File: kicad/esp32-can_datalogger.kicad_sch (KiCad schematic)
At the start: 22 parts, among them J1 USB_C_Receptacle_USB2.0_16P, J2 USB_C_Receptacle_USB2.0_16P, J3 USB_C_Receptacle_USB2.0_16P, J4 USB_C_Receptacle_USB2.0_16P, J5 MSD-4-A, U5 TJA1051T, U6 TJA1051T

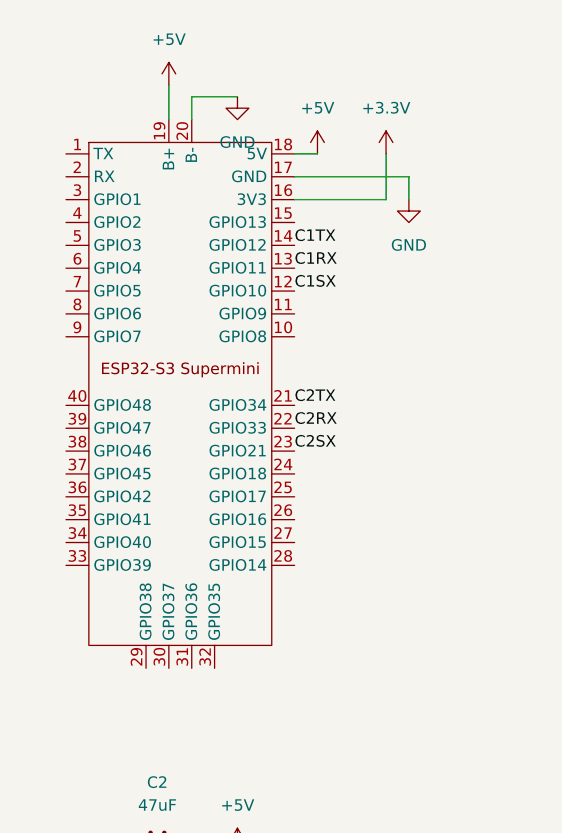
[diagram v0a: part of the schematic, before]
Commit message: switch to esp32-c6
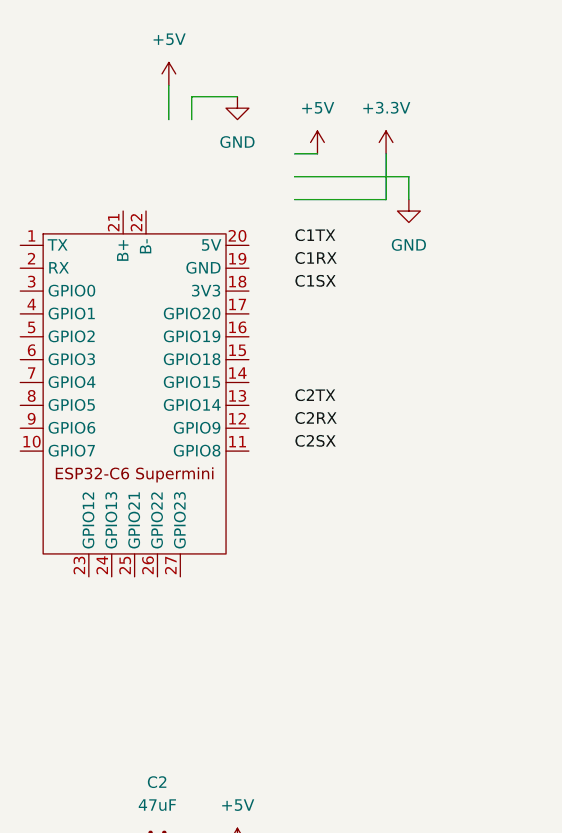
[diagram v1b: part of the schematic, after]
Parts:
- removed U1: (no value), esp32-can_datalogger:ESP32-S3 Supermini, symbol esp32-can_datalogger:esp32-s3-supermini
- added U1: (no value), esp32-can_datalogger:ESP32-C6 Supermini, symbol esp32-can_datalogger:esp32-c6-supermini
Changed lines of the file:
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@@
+	)
+	(symbol
+		(lib_id "esp32-can_datalogger:esp32-c6-supermini")
+		(at 31.75 57.15 0)
+		(unit 1)
+		(body_style 1)
+		(exclude_from_sim no)
+		(in_bom yes)
+		(on_board yes)
+		(in_pos_files yes)
+		(dnp no)
+		(fields_autoplaced yes)
+		(property "Reference" "U1"
+			(at 31.75 62.23 0)
+			(hide yes)
+			(show_name no)
+			(do_not_autoplace no)
+			(effects
+				(font
+					(size 1.27 1.27)
+				)
+			)
+		)
+		(property "Value" ""
+			(at 31.75 62.23 0)
+			(hide yes)
+			(show_name no)
+			(do_not_autoplace no)
+			(effects
+				(font
+					(size 1.27 1.27)
+				)
+			)
+		)
+		(property "Footprint" "esp32-can_datalogger:ESP32-C6 Supermini"
+			(at 31.75 62.23 0)
+			(hide yes)
+			(show_name no)
+			(do_not_autoplace no)
+			(effects
+				(font
+					(size 1.27 1.27)
+				)
+			)
+		)
+		(property "Datasheet" ""
+			(at 31.75 62.23 0)
+			(hide yes)
+			(show_name no)
+			(do_not_autoplace no)
+			(effects
+				(font
+					(size 1.27 1.27)
+				)
+			)
+		)
+		(property "Description" ""
+			(at 31.75 62.23 0)
+			(hide yes)
+			(show_name no)
+			(do_not_autoplace no)
+			(effects
+				(font
+					(size 1.27 1.27)
+				)
+			)
+		)
+		(pin "4"
+		)
+		(pin "5"
+		)
+		(pin "24"
+		)
+		(pin "26"
+		)
+		(pin "7"
+		)
+		(pin "21"
+		)
+		(pin "22"
+		)
+		(pin "12"
+		)
+		(pin "16"
+		)
+		(pin "27"
+		)
+		(pin "20"
+		)
+		(pin "17"
+		)
+		(pin "6"
+		)
+		(pin "9"
+		)
+		(pin "11"
+		)
+		(pin "13"
+		)
+		(pin "15"
+		)
+		(pin "19"
+		)
+		(pin "23"
+		)
+		(pin "10"
+		)
+		(pin "14"
+		)
+		(pin "18"
+		)
+		(pin "8"
+		)
+		(pin "25"
+		)
+		(pin "2"
+		)
+		(pin "3"
+		)
+		(pin "1"
+		)
+		(instances
+			(project "esp32-can_datalogger"
+				(path "/27d88dad-6a90-4f6f-a0dd-ec7ff61f0111"
+					(reference "U1")
+					(unit 1)
+				)
+			)
+		)
 	)
 	(symbol
@@
 					(unit 1)
 				)
-			)
-		)
-	)
-	(symbol
-		(lib_id "esp32-can_datalogger:esp32-s3-supermini")
-		(at 36.83 54.61 0)
-		(unit 1)
-		(body_style 1)
-		(exclude_from_sim no)
-		(in_bom yes)
-		(on_board yes)
-		(in_pos_files yes)
-		(dnp no)
-		(fields_autoplaced yes)
-		(property "Reference" "U1"
-			(at 36.83 52.07 0)
-			(hide yes)
-			(show_name no)
-			(do_not_autoplace no)
-			(effects
-				(font
-					(size 1.27 1.27)
-				)
-			)
-		)
-		(property "Value" ""
-			(at 36.83 52.07 0)
-			(hide yes)
-			(show_name no)
-			(do_not_autoplace no)
-			(effects
-				(font
-					(size 1.27 1.27)
-				)
-			)
-		)
-		(property "Footprint" "esp32-can_datalogger:ESP32-S3 Supermini"
-			(at 36.83 52.07 0)
-			(hide yes)
-			(show_name no)
-			(do_not_autoplace no)
-			(effects
-				(font
-					(size 1.27 1.27)
-				)
-			)
-		)
-		(property "Datasheet" ""
-			(at 36.83 52.07 0)
-			(hide yes)
-			(show_name no)
-			(do_not_autoplace no)
-			(effects
-				(font
-					(size 1.27 1.27)
-				)
-			)
-		)
-		(property "Description" ""
-			(at 36.83 52.07 0)
-			(hide yes)
-			(show_name no)
-			(do_not_autoplace no)
-			(effects
-				(font
-					(size 1.27 1.27)
-				)
-			)
-		)
-		(pin "19"
-		)
-		(pin "9"
-		)
-		(pin "13"
-		)
-		(pin "14"
-		)
-		(pin "10"
-		)
-		(pin "6"
-		)
-		(pin "5"
-		)
-		(pin "2"
-		)
-		(pin "4"
-		)
-		(pin "3"
-		)
-		(pin "1"
-		)
-		(pin "7"
-		)
-		(pin "11"
-		)
-		(pin "12"
-		)
-		(pin "15"
-		)
-		(pin "16"
-		)
-		(pin "17"
-		)
-		(pin "18"
-		)
-		(pin "8"
-		)
-		(pin "29"
-		)
-		(pin "21"
-		)
-		(pin "26"
-		)
-		(pin "20"
-		)
-		(pin "28"
-		)
-		(pin "23"
-		)
-		(pin "27"
-		)
-		(pin "22"
-		)
-		(pin "24"
-		)
-		(pin "25"
-		)
-		(pin "30"
-		)
-		(pin "32"
-		)
-		(pin "33"
-		)
-		(pin "35"
-		)
-		(pin "34"
-		)
-		(pin "36"
-		)
-		(pin "31"
-		)
-		(pin "40"
-		)
-		(pin "37"
-		)
-		(pin "39"
-		)
-		(pin "38"
-		)
-		(instances
-			(project "esp32-can_datalogger"
-				(path "/27d88dad-6a90-4f6f-a0dd-ec7ff61f0111"
-					(reference "U1")
-					(unit 1)
-				)

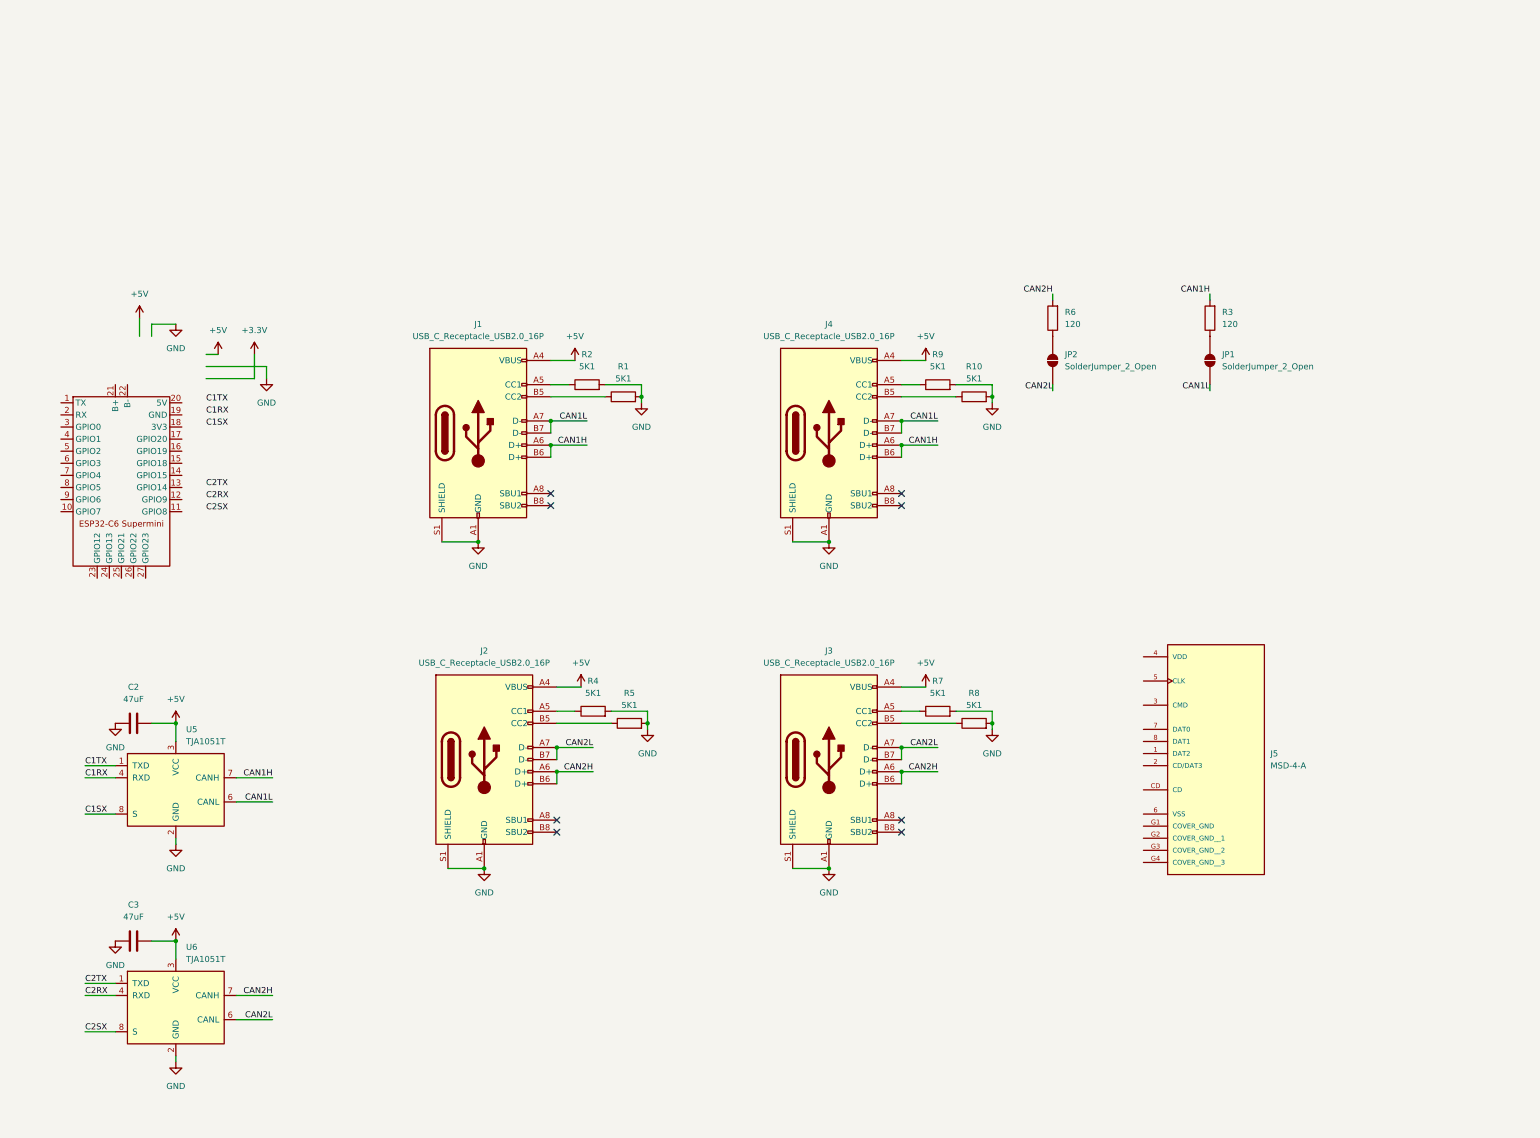
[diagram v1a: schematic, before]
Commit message: add gps, imu to board schematic
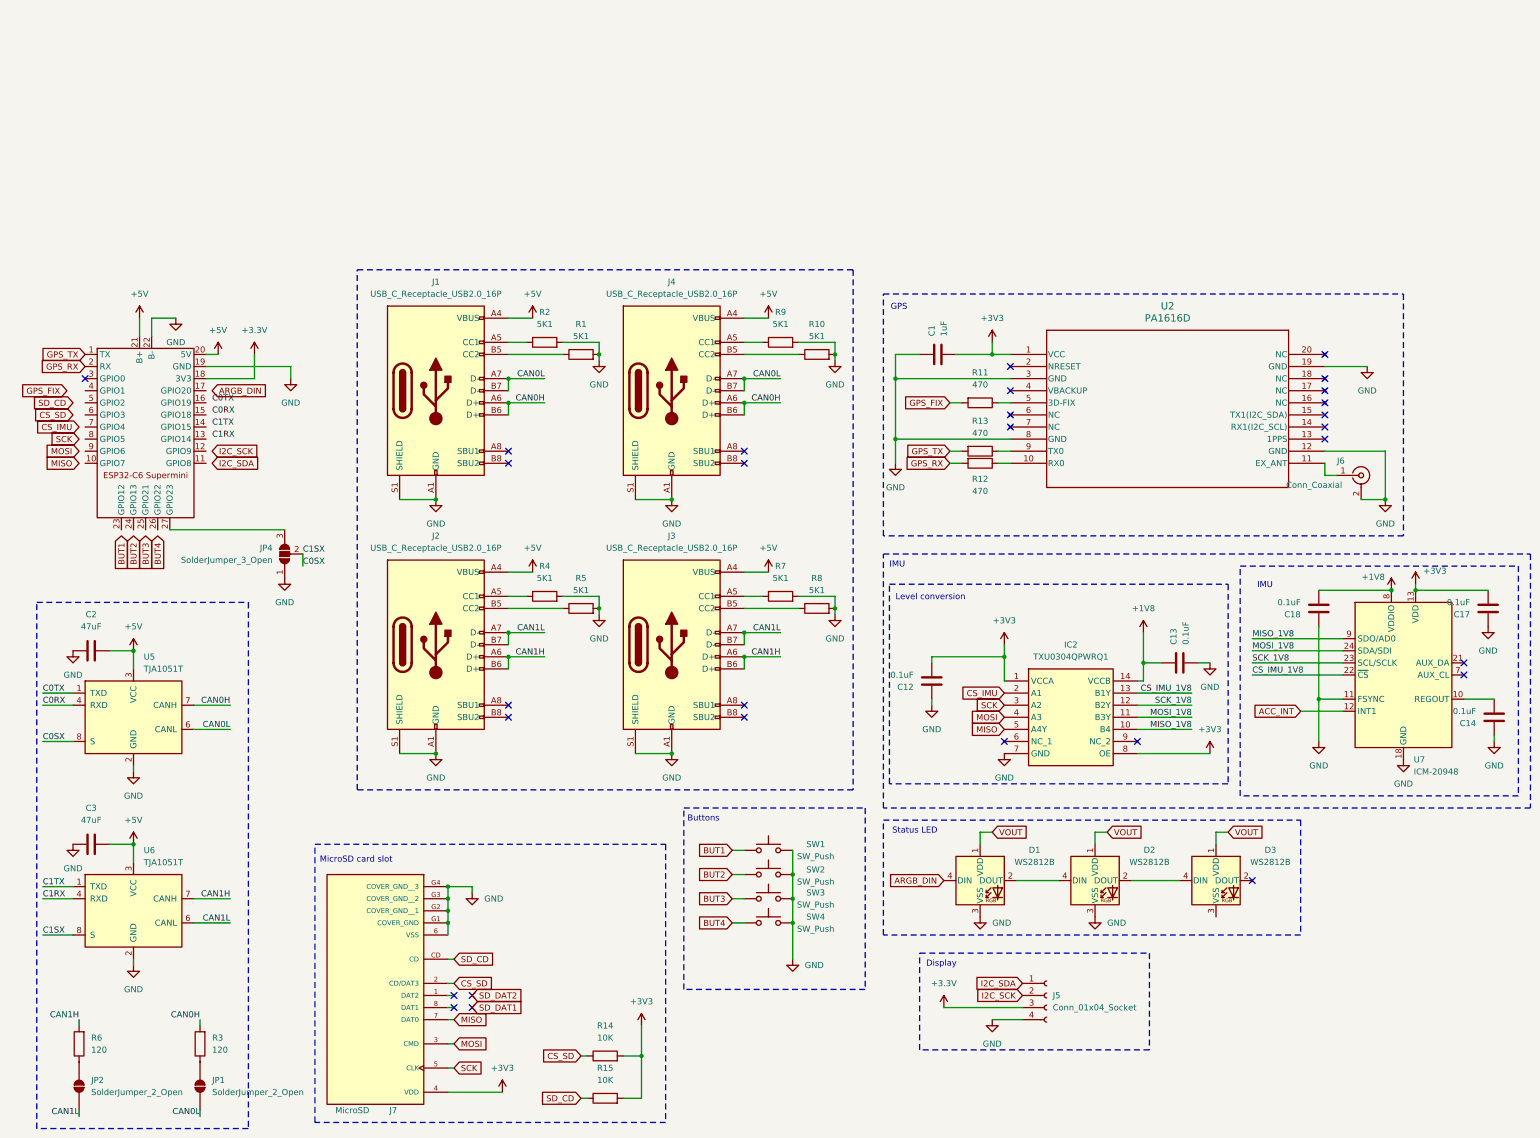
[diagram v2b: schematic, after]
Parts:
- removed J5: MSD-4-A, esp32-can_datalogger:CUI_MSD-4-A, symbol esp32-can_datalogger:MSD-4-A
- added C1: 1uF, Capacitor_SMD:C_1206_3216Metric, symbol Device:C
- added C12, C13, C14, C17, C18: 0.1uF, Capacitor_SMD:C_1206_3216Metric, symbol Device:C
- added D1, D2, D3: WS2812B, LED_SMD:LED_WS2812B_PLCC4_5.0x5.0mm_P3.2mm, symbol LED:WS2812B
- added IC2: TXU0304QPWRQ1, esp32-gps-lib:SOP65P640X120-14N, symbol esp32-gps-lib:TXU0304QPWRQ1
- added J5: Conn_01x04_Socket, symbol Connector:Conn_01x04_Socket
- added J6: Conn_Coaxial, Connector_Coaxial:U.FL_Hirose_U.FL-R-SMT-1_Vertical, symbol Connector:Conn_Coaxial
- added J7: MicroSD, esp32-gps-lib:CUI_MSD-4-A, symbol esp32-gps-lib:MSD-4-A
- added JP4: SolderJumper_3_Open, symbol Jumper:SolderJumper_3_Open
- added R11, R12, R13: 470, Resistor_SMD:R_1206_3216Metric, symbol Device:R
- added R14, R15: 10K, Resistor_SMD:R_1206_3216Metric, symbol Device:R
- added SW1, SW2, SW3, SW4: SW_Push, Button_Switch_SMD:SW_Push_SPST_NO_Alps_SKRK, symbol Switch:SW_Push
- added U2: PA1616D, esp32-gps-lib:CD-PA1616D_ADA, symbol esp32-gps-lib:5186
- added U7: ICM-20948, Sensor_Motion:InvenSense_QFN-24_3x3mm_P0.4mm, symbol Sensor_Motion:ICM-20948
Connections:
- net C2RX is gone; now on net C1RX: U6.4 (RXD)
- net C2SX is gone; now on net C0SX: U6.8 (S)
- net C2TX is gone; now on net C1TX: U6.1 (TXD)
- net CAN2H is gone; now on net CAN1H: J2.A6 (D+), J2.B6 (D+), J3.A6 (D+), J3.B6 (D+), R6.2, U6.7 (CANH)
- net CAN2L is gone; now on net CAN1L: J2.A7 (D-), J2.B7 (D-), J3.A7 (D-), J3.B7 (D-), JP2.1 (A), U6.6 (CANL)
- net +3.3V: now also U1.18 (3V3), J5.3 (Pin_3)
- net +5V: now also U1.20 (5V), U1.21 (B+)
- net C1RX: no longer U5.4 (RXD)
- net C1TX: no longer U5.1 (TXD)
- net CAN1H: no longer J1.A6 (D+), J1.B6 (D+), J4.A6 (D+), J4.B6 (D+), R3.2, U5.7 (CANH)
- net CAN1L: no longer J1.A7 (D-), J1.B7 (D-), J4.A7 (D-), J4.B7 (D-), JP1.1 (A), U5.6 (CANL)
- net GND: now also U1.19 (GND), U1.22 (B-), C1.1, C12.1, C13.2, C14.1, C17.1, C18.1, D1.3 (VSS), D2.3 (VSS), IC2.7 (GND), J5.4 (Pin_4), J6.2 (Ext), J7.6 (VSS), J7.G1 (COVER_GND), J7.G2 (COVER_GND__1), J7.G3 (COVER_GND__2), J7.G4 (COVER_GND__3), JP4.1 (A), SW1.2, SW2.2, SW3.2, SW4.2, U2.12 (GND), U2.19 (GND), U2.3 (GND), U2.8 (GND), U7.11 (FSYNC), U7.18 (GND), U7.20 (GND)
- net GPS_TX: now reaches U1.1 (TX)
- net GPS_TX: now also R13.2
- net GPS_RX: now reaches U1.2 (RX)
- net GPS_RX: now also R12.2
- net at U1.27 (GPIO23): now also JP4.3 (B)
- net C1SX renamed C0SX
- net C0SX: now also JP4.2 (C)
- new net: D2.2 (DOUT), D3.4 (DIN)
- new net: D1.2 (DOUT), D2.4 (DIN)
- new net: J6.1 (In), U2.11 (EX_ANT)
- new net: C14.2, U7.10 (REGOUT)
- new net: R12.1, U2.10 (RX0)
- new net: R11.1, U2.5 (3D-FIX)
- new net: R13.1, U2.9 (TX0)
- new net +1V8: C13.1, C18.2, IC2.14 (VCCB), U7.8 (VDDIO)
- new net +3V3: C1.2, C12.2, C17.2, IC2.1 (VCCA), IC2.8 (OE), J7.4 (VDD), R14.2, R15.2, U2.1 (VCC), U7.13 (VDD)
- new net ACC_INT: U7.12 (INT1)
- new net ARGB_DIN: D1.4 (DIN)
- new net BUT1: SW1.1
- new net BUT2: SW2.1
- new net BUT3: SW3.1
- new net BUT4: SW4.1
- new net C0RX: U5.4 (RXD)
- new net C0TX: U5.1 (TXD)
- new net CAN0H: J1.A6 (D+), J1.B6 (D+), J4.A6 (D+), J4.B6 (D+), R3.2, U5.7 (CANH)
- new net CAN0L: J1.A7 (D-), J1.B7 (D-), J4.A7 (D-), J4.B7 (D-), JP1.1 (A), U5.6 (CANL)
- new net CS_IMU: IC2.2 (A1)
- new net CS_IMU_1V8: IC2.13 (B1Y), U7.22 (~{CS})
- new net CS_SD: J7.2 (CD/DAT3), R14.1
- new net GPS_FIX: R11.2
- new net I2C_SCK: J5.2 (Pin_2)
- new net I2C_SDA: J5.1 (Pin_1)
- new net MISO: IC2.5 (A4Y), J7.7 (DAT0)
- new net MISO_1V8: IC2.10 (B4), U7.9 (SDO/AD0)
- new net MOSI: IC2.4 (A3), J7.3 (CMD)
- new net MOSI_1V8: IC2.11 (B3Y), U7.24 (SDA/SDI)
- new net SCK: IC2.3 (A2), J7.5 (CLK)
- new net SCK_1V8: IC2.12 (B2Y), U7.23 (SCL/SCLK)
- new net SD_CD: J7.CD, R15.1
- new net VOUT: D1.1 (VDD), D2.1 (VDD), D3.1 (VDD)
- no-connect marks 8 -> 29
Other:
- note added: "Buttons"
- note added: "Display"
- note added: "GPS"
- note added: "IMU"
- note added: "Level conversion"
- note added: "MicroSD card slot"
- note added: "Status LED"
- moved on the sheet: C2, C3, J1, J2, J3, J4, JP1, JP2, R1, R10, R2, R3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
